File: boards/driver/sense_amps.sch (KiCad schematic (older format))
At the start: 96 parts

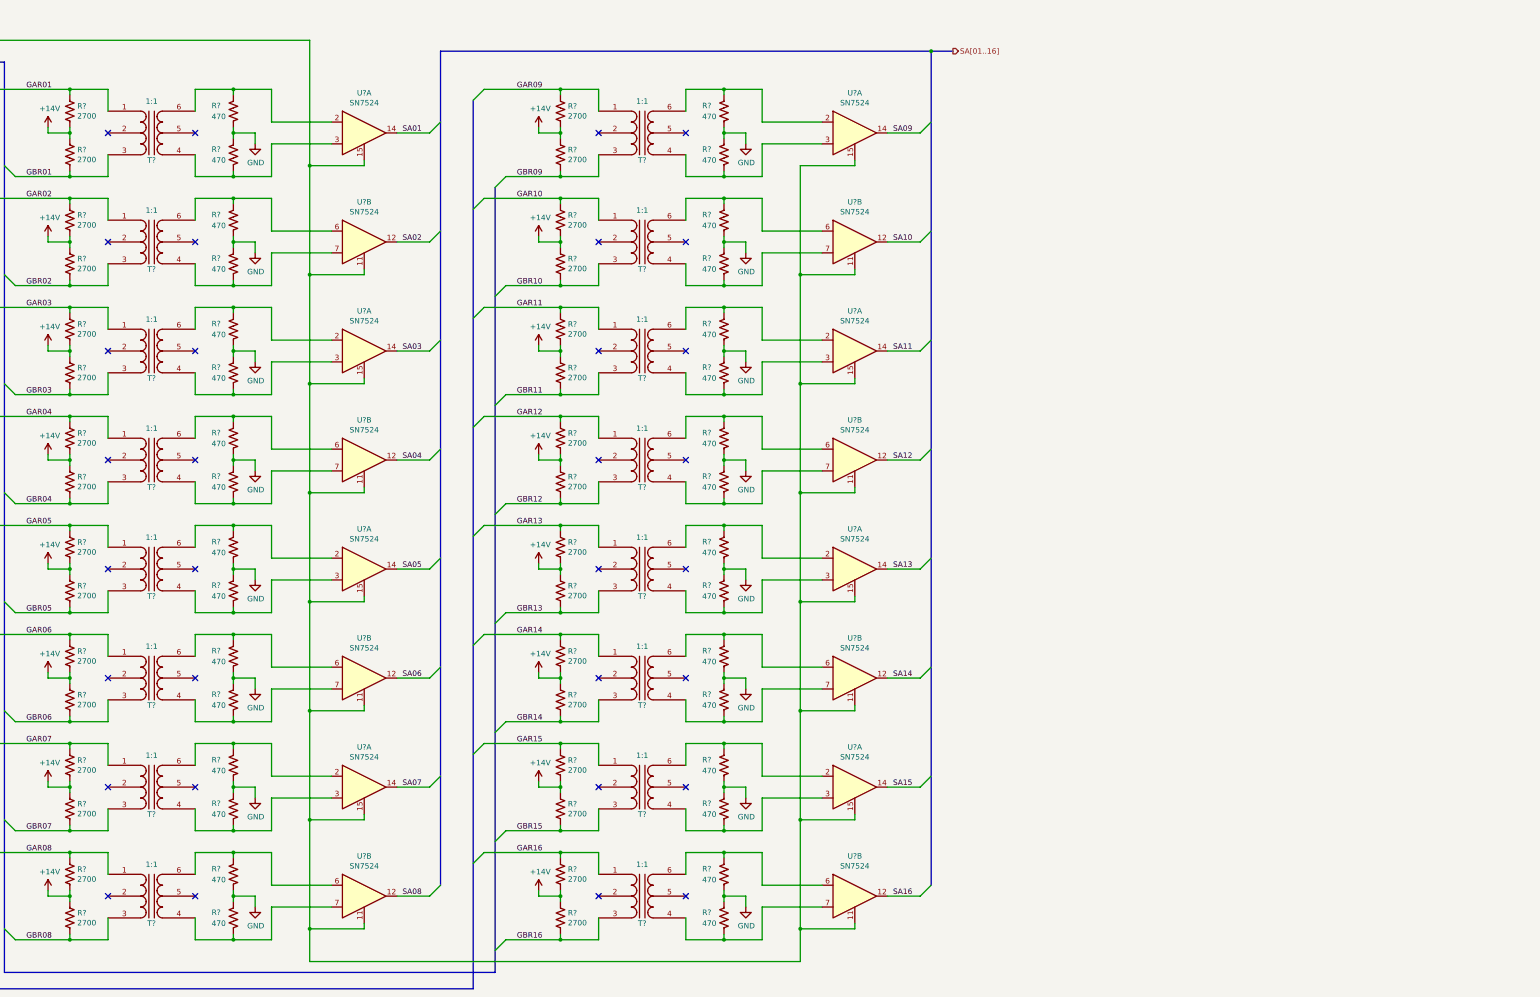
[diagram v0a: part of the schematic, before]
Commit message: Added a sheet containing all of the required current drivers to the interface board
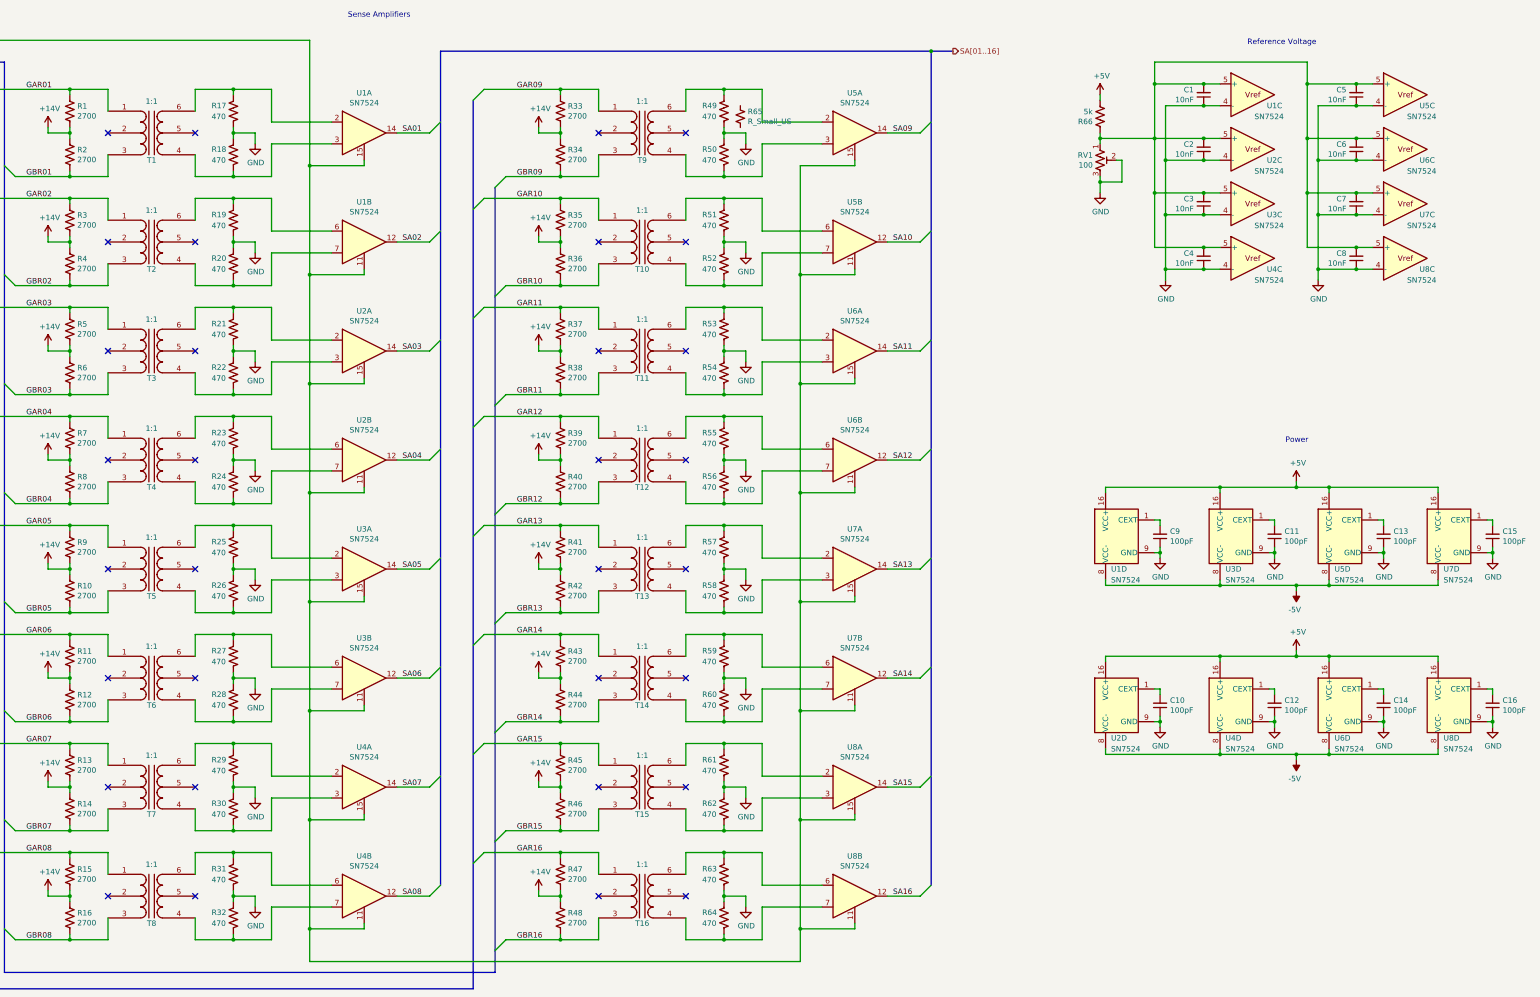
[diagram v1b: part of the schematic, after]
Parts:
- added C1, C2, C3, C4, C5, C6, C7, C8: 10nF, symbol Device:C_Small
- added C10, C11, C12, C13, C14, C15, C16, C9: 100pF, symbol Device:C_Small
- added R65: R_Small_US, symbol Device:R_Small_US
- added R66: 5k, symbol Device:R_US
- added RV1: 100, symbol Device:R_POT_TRIM_US
- added unit 3 of U1
- added unit 4 of U1
- added unit 3 of U2
- added unit 4 of U2
- added unit 3 of U3
- added unit 4 of U3
- added unit 3 of U4
- added unit 4 of U4
- added unit 3 of U5
- added unit 4 of U5
- added unit 3 of U6
- added unit 4 of U6
- added unit 3 of U7
- added unit 4 of U7
- added unit 3 of U8
- added unit 4 of U8
- gave numbers to parts that had none: 88
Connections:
- net GND: now also C1.1, C10.1, C11.1, C12.1, C13.1, C14.1, C15.1, C16.1, C2.1, C3.1, C4.1, C5.1, C6.1, C7.1, C8.1, C9.1, RV1.2, RV1.3, U1.13 (GND), U1.4 (-), U1.9 (GND), U2.13 (GND), U2.4 (-), U2.9 (GND), U3.13 (GND), U3.4 (-), U3.9 (GND), U4.13 (GND), U4.4 (-), U4.9 (GND), U5.13 (GND), U5.4 (-), U5.9 (GND), U6.13 (GND), U6.4 (-), U6.9 (GND), U7.13 (GND), U7.4 (-), U7.9 (GND), U8.13 (GND), U8.4 (-), U8.9 (GND)
- new net: C1.2, C2.2, C3.2, C4.2, C5.2, C6.2, C7.2, C8.2, R66.1, RV1.1, U1.5 (+), U2.5 (+), U3.5 (+), U4.5 (+), U5.5 (+), U6.5 (+), U7.5 (+), U8.5 (+)
- new net: C9.2, U1.1 (CEXT)
- new net: C11.2, U3.1 (CEXT)
- new net: C13.2, U5.1 (CEXT)
- new net: C15.2, U7.1 (CEXT)
- new net: C10.2, U2.1 (CEXT)
- new net: C12.2, U4.1 (CEXT)
- new net: C14.2, U6.1 (CEXT)
- new net: C16.2, U8.1 (CEXT)
- new net +5V: R66.2, U1.16 (VCC+), U2.16 (VCC+), U3.16 (VCC+), U4.16 (VCC+), U5.16 (VCC+), U6.16 (VCC+), U7.16 (VCC+), U8.16 (VCC+)
- new net -5V: U1.8 (VCC-), U2.8 (VCC-), U3.8 (VCC-), U4.8 (VCC-), U5.8 (VCC-), U6.8 (VCC-), U7.8 (VCC-), U8.8 (VCC-)
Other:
- note added: "Power"
- note added: "Reference Voltage"
- note added: "Sense Amplifiers"

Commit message: Completely overhauled rope driver circuitry to much, much more closely resemble the original.
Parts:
- removed R65: R_Small_US, symbol Device:R_Small_US
- R1, R10, R11, R12, R13, R14, R15, R16, R2, R3, R33, R34, R35, R36, R37, R38, R39, R4, R40, R41, R42, R43, R44, R45, R46, R47, R48, R5, R6, R7, R8, R9: value 2700 -> 2.7k; footprint (none) -> Resistor_SMD:R_1206_3216Metric
- R17, R18, R19, R20, R21, R22, R23, R24, R25, R26, R27, R28, R29, R30, R31, R32, R49, R50, R51, R52, R53, R54, R55, R56, R57, R58, R59, R60, R61, R62, R63, R64: footprint (none) -> Resistor_SMD:R_1206_3216Metric
- R65: renamed from R66; footprint (none) -> Resistor_SMD:R_1206_3216Metric
- U1, U2, U3, U4, U5, U6, U7, U8: footprint (none) -> Package_DIP:DIP-10_W7.62mm
- renumbered C9 to C1, C6 to C10, C7 to C11, C8 to C12, C10 to C2, C1 to C3, C2 to C4, C3 to C5, C4 to C6, C11 to C7, C12 to C8, C5 to C9
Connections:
- net +14V renamed BPLSWX
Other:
- moved on the sheet: C1, C13, C14, C15, C16, C2, C7, C8, U1D, U2D, U3D, U4D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

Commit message: Driver board: a bit more schematic work and some initial footprint selections
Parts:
- R1, R10, R11, R12, R13, R14, R15, R16, R17, R18, R19, R2, R20, R21, R22, R23, R24, R25, R26, R27, R28, R29, R3, R30, R31, R32, R33, R34, R35, R36, R37, R38, R39, R4, R40, R41, R42, R43, R44, R45, R46, R47, R48, R49, R5, R50, R51, R52, R53, R54, R55, R56, R57, R58, R59, R6, R60, R61, R62, R63, R64, R65, R7, R8, R9: footprint Resistor_SMD:R_1206_3216Metric -> Resistor_SMD:R_0603_1608Metric

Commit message: Driver board: finished first rough draft schematic. Lots of placeholders, but at least every place is held.
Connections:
- net GAR01 renamed GAR1
- net GAR02 renamed GAR2
- net GAR03 renamed GAR3
- net GAR04 renamed GAR4
- net GAR05 renamed GAR5
- net GAR06 renamed GAR6
- net GAR07 renamed GAR7
- net GAR08 renamed GAR8
- net GAR09 renamed GAR9
- net GBR01 renamed GBR1
- net GBR02 renamed GBR2
- net GBR03 renamed GBR3
- net GBR04 renamed GBR4
- net GBR05 renamed GBR5
- net GBR06 renamed GBR6
- net GBR07 renamed GBR7
- net GBR08 renamed GBR8
- net GBR09 renamed GBR9
- net SA01 renamed SA1
- net SA02 renamed SA2
- net SA03 renamed SA3
- net SA04 renamed SA4
- net SA05 renamed SA5
- net SA06 renamed SA6
- net SA07 renamed SA7
- net SA08 renamed SA8
- net SA09 renamed SA9
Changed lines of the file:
@@
 $Descr USLedger 17000 11000
 encoding utf-8
-Sheet 2 68
+Sheet 2 69
 Title ""
 Date ""
@@
 	1600 2350 1700 2450
 Text Label 1800 1650 0    50   ~ 0
-GAR01
+GAR1
 Text Label 1800 2450 0    50   ~ 0
-GBR01
+GBR1
 NoConn ~ 2550 2050
 NoConn ~ 3350 2050
@@
 	1600 3350 1700 3450
 Text Label 1800 2650 0    50   ~ 0
-GAR02
+GAR2
 Text Label 1800 3450 0    50   ~ 0
-GBR02
+GBR2
 NoConn ~ 2550 3050
 NoConn ~ 3350 3050
@@
 	1600 4350 1700 4450
 Text Label 1800 3650 0    50   ~ 0
-GAR03
+GAR3
 Text Label 1800 4450 0    50   ~ 0
-GBR03
+GBR3
 NoConn ~ 2550 4050
 NoConn ~ 3350 4050
@@
 	1600 5350 1700 5450
 Text Label 1800 4650 0    50   ~ 0
-GAR04
+GAR4
 Text Label 1800 5450 0    50   ~ 0
-GBR04
+GBR4
 NoConn ~ 2550 5050
 NoConn ~ 3350 5050
@@
 	1600 6350 1700 6450
 Text Label 1800 5650 0    50   ~ 0
-GAR05
+GAR5
 Text Label 1800 6450 0    50   ~ 0
-GBR05
+GBR5
 NoConn ~ 2550 6050
 NoConn ~ 3350 6050
@@
 	1600 7350 1700 7450
 Text Label 1800 6650 0    50   ~ 0
-GAR06
+GAR6
 Text Label 1800 7450 0    50   ~ 0
-GBR06
+GBR6
 NoConn ~ 2550 7050
 NoConn ~ 3350 7050
@@
 	1600 8350 1700 8450
 Text Label 1800 7650 0    50   ~ 0
-GAR07
+GAR7
 Text Label 1800 8450 0    50   ~ 0
-GBR07
+GBR7
 NoConn ~ 2550 8050
 NoConn ~ 3350 8050
@@
 	1600 9350 1700 9450
 Text Label 1800 8650 0    50   ~ 0
-GAR08
+GAR8
 Text Label 1800 9450 0    50   ~ 0
-GBR08
+GBR8
 NoConn ~ 2550 9050
 NoConn ~ 3350 9050
@@
 	6200 2450 6100 2550
 Text Label 6300 1650 0    50   ~ 0
-GAR09
+GAR9
 Text Label 6300 2450 0    50   ~ 0
-GBR09
+GBR9
 NoConn ~ 7050 2050
 NoConn ~ 7850 2050
@@
 SBF
 Text HLabel 1250 1300 0    50   Input ~ 0
-GAR[01..16]
+GAR[1..16]
 Text HLabel 1250 1400 0    50   Input ~ 0
-GBR[01..16]
+GBR[1..16]
 Wire Wire Line
 	5200 2050 5500 2050
 Text Label 5250 2050 0    50   ~ 0
-SA01
+SA1
 Entry Wire Line
 	5500 2050 5600 1950
@@
 	5200 3050 5500 3050
 Text Label 5250 3050 0    50   ~ 0
-SA02
+SA2
 Entry Wire Line
 	5500 3050 5600 2950
@@
 	5200 4050 5500 4050
 Text Label 5250 4050 0    50   ~ 0
-SA03
+SA3
 Entry Wire Line
 	5500 4050 5600 3950
@@
 	5200 5050 5500 5050
 Text Label 5250 5050 0    50   ~ 0
-SA04
+SA4
 Entry Wire Line
 	5500 5050 5600 4950
@@
 	5200 6050 5500 6050
 Text Label 5250 6050 0    50   ~ 0
-SA05
+SA5
 Entry Wire Line
 	5500 6050 5600 5950
@@
 	5200 7050 5500 7050
 Text Label 5250 7050 0    50   ~ 0
-SA06
+SA6
 Entry Wire Line
 	5500 7050 5600 6950
@@
 	5200 8050 5500 8050
 Text Label 5250 8050 0    50   ~ 0
-SA07
+SA7
 Entry Wire Line
 	5500 8050 5600 7950
@@
 	5200 9050 5500 9050
 Text Label 5250 9050 0    50   ~ 0
-SA08
+SA8
 Entry Wire Line
 	5500 9050 5600 8950
@@
 	9700 2050 10000 2050
 Text Label 9750 2050 0    50   ~ 0
-SA09
+SA9
 Entry Wire Line
 	10000 2050 10100 1950
@@
 Connection ~ 10100 1300
 Text HLabel 10300 1300 2    50   Output ~ 0
-SA[01..16]
+SA[1..16]
 $Comp
 L lachesis:SN7524 U?

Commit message: Driver board: fleshed out the hotswap controller, tweaked some resistors, and added some bypass caps
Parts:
- added C11, C12, C13, C14, C21, C22, C23, C24, C25, C26, C29, C30, C31, C32, C7, C8: 0.1uF, symbol Device:C_Small
- renumbered C8 to C10, C9 to C15, C10 to C16, C11 to C17, C12 to C18, C13 to C19, C14 to C20, C15 to C27, C16 to C28, C7 to C9
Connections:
- net +5V: now also C11.1, C13.1, C21.1, C23.1, C25.1, C29.1, C31.1, C7.1
- net -5V: now also C12.2, C14.2, C22.2, C24.2, C26.2, C30.2, C32.2, C8.2
- net GND: now also C11.2, C12.1, C13.2, C14.1, C21.2, C22.1, C23.2, C24.1, C25.2, C26.1, C29.2, C30.1, C31.2, C32.1, C7.2, C8.1
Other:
- moved on the sheet: C1, C10, C19, C2, C20, C27, C28, C9, U1D, U2D, U3D, U4D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

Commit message: Driver board: significant cleanup. Moved sense amp pairs into a subsheet, split tuning resistors into two globally, pushed input circuits into their corresponding sheets.
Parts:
- removed C1, C10, C19, C2, C20, C27, C28, C9: 100pF, symbol Device:C_Small
- removed C11, C12, C13, C14, C21, C22, C23, C24, C25, C26, C29, C30, C31, C32, C7, C8: 0.1uF, symbol Device:C_Small
- removed C15, C16, C17, C18, C3, C4, C5, C6: 10nF, symbol Device:C_Small
- removed R10, R11, R12, R13, R14, R15, R16, R3, R33, R34, R35, R36, R37, R38, R39, R4, R40, R41, R42, R43, R44, R45, R46, R47, R48, R5, R6, R7, R8, R9: 2.7k, Resistor_SMD:R_0603_1608Metric, symbol Device:R_US
- removed R17, R18, R19, R20, R21, R22, R23, R24, R25, R26, R27, R28, R29, R30, R31, R32, R49, R50, R51, R52, R53, R54, R55, R56, R57, R58, R59, R60, R61, R62, R63, R64: 470, Resistor_SMD:R_0603_1608Metric, symbol Device:R_US
- removed R65: 5k, Resistor_SMD:R_0603_1608Metric, symbol Device:R_US
- removed RV1: 100, symbol Device:R_POT_TRIM_US
- removed T1, T10, T11, T12, T13, T14, T15, T16, T2, T3, T4, T5, T6, T7, T8, T9: 1:1, symbol lachesis:Transformer_SP_SS
- removed U1, U2, U3, U4, U5, U6, U7, U8: SN7524, Package_DIP:DIP-10_W7.62mm, symbol lachesis:SN7524
- added C1: 4.7uF, symbol Device:C
- added C2: 1uF, symbol Device:C
- added U1: AD1582BRTZ, symbol lachesis:AD1582
- R1: value 2.7k -> 1.27k; footprint Resistor_SMD:R_0603_1608Metric -> (none)
- R2: value 2.7k -> 249; footprint Resistor_SMD:R_0603_1608Metric -> (none)
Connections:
- net +5V: now also C1.2, U1.3 (VIN)
- net BPLSWX: no longer R1.2, R2.1
- net GAR1: no longer R1.1
- net GBR1: no longer R2.2
- net GND: now also R2.2, C1.1, C2.2, U1.2 (GND)
- new net: C2.1, R1.1, U1.1 (VOUT)
- new net VREF: R1.2, R2.1
- no-connect marks 32 -> 0
